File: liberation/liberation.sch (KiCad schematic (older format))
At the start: 18 parts

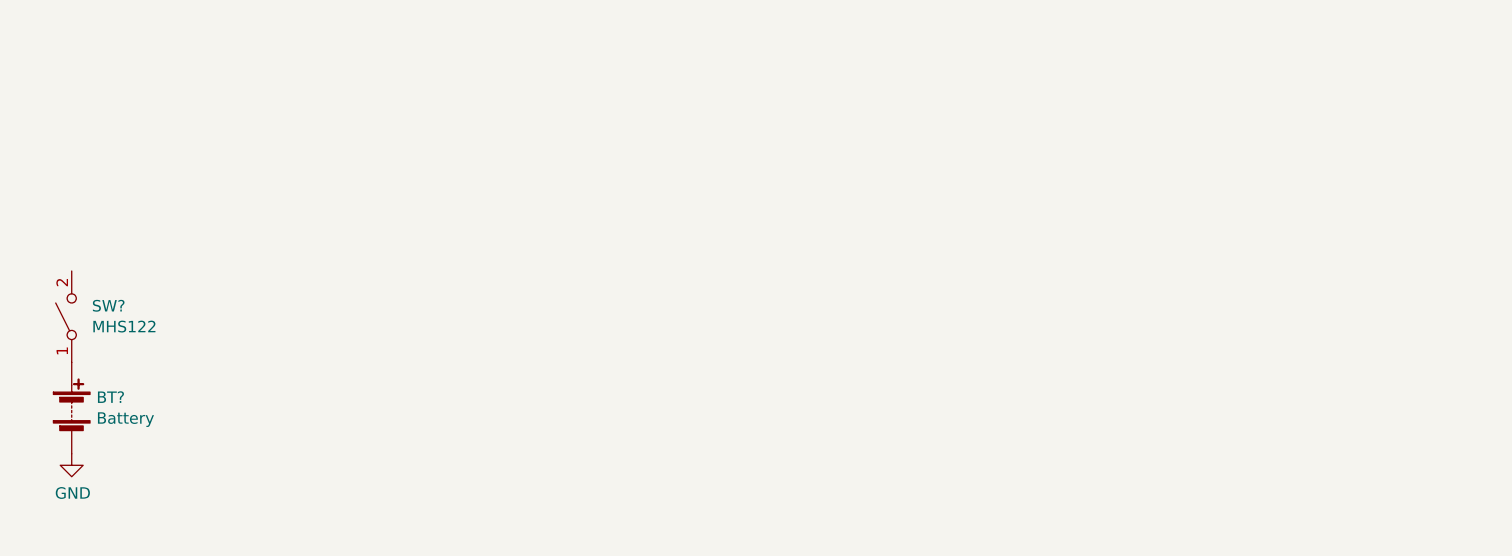
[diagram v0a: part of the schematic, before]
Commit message: boost converter sircuit
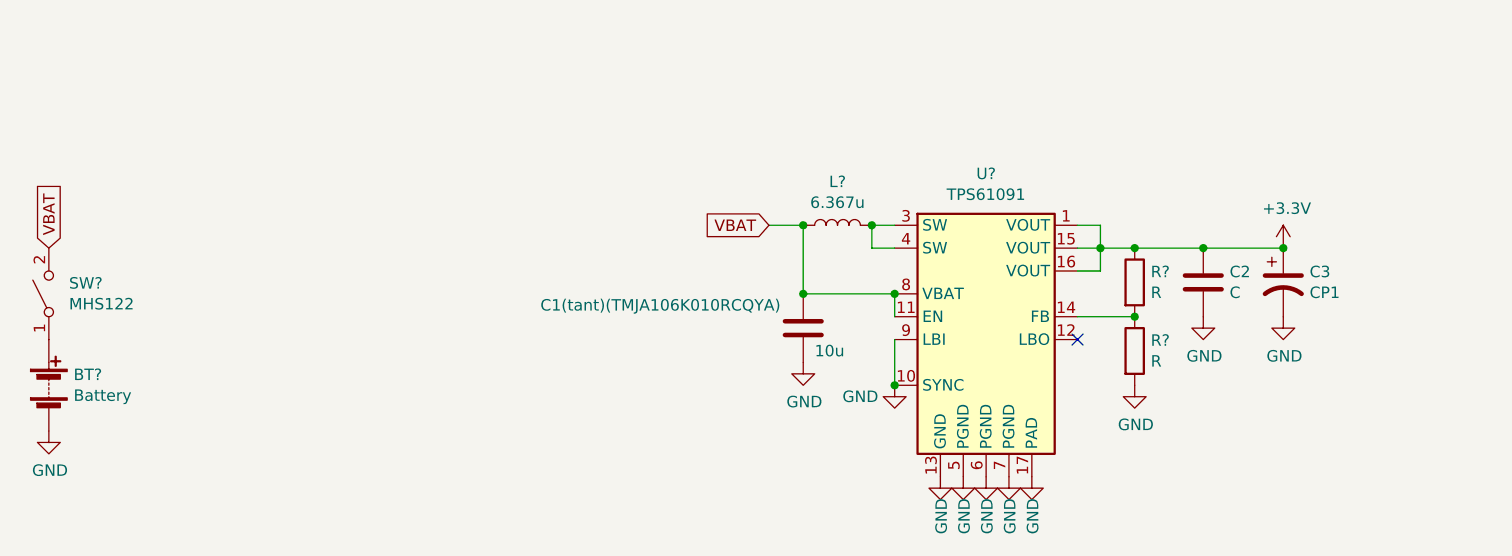
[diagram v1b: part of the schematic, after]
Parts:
- added C1(tant)(TMJA106K010RCQYA): 10u, symbol Device:C
- added C2: C, symbol Device:C
- added C3: CP1, symbol Device:CP1
- added L?: 6.367u, symbol Device:L
- added R? (x2): R, symbol Device:R
- added U?: TPS61091, Package_DFN_QFN:Texas_S-PVQFN-N16_EP2.7x2.7mm_ThermalVias, symbol Regulator_Switching:TPS61091
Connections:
- net +3V3: now also C2.1, C3.1, R?.1, U?.1 (VOUT), U?.15 (VOUT), U?.16 (VOUT)
- net GND: now also C1(tant)(TMJA106K010RCQYA).2, C2.2, C3.2, R?.2, U?.10 (SYNC), U?.13 (GND), U?.17 (PAD), U?.5 (PGND), U?.6 (PGND), U?.7 (PGND), U?.9 (LBI)
- net VBAT: now reaches SW?.2 (B)
- net VBAT: now also C1(tant)(TMJA106K010RCQYA).1, L?.1, U?.11 (EN), U?.8 (VBAT)
- new net: R?.1, R?.2, U?.14 (FB)
- new net: L?.2, U?.3 (SW), U?.4 (SW)
- no-connect marks 0 -> 1
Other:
- moved on the sheet: BT?, SW?
